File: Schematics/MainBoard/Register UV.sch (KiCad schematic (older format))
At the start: 13 parts, among them J27 UV LED Connector, U14 74F161, U15 74LS245, U16 74F161, U17 74LS245, U24 74F161, U25 74F161

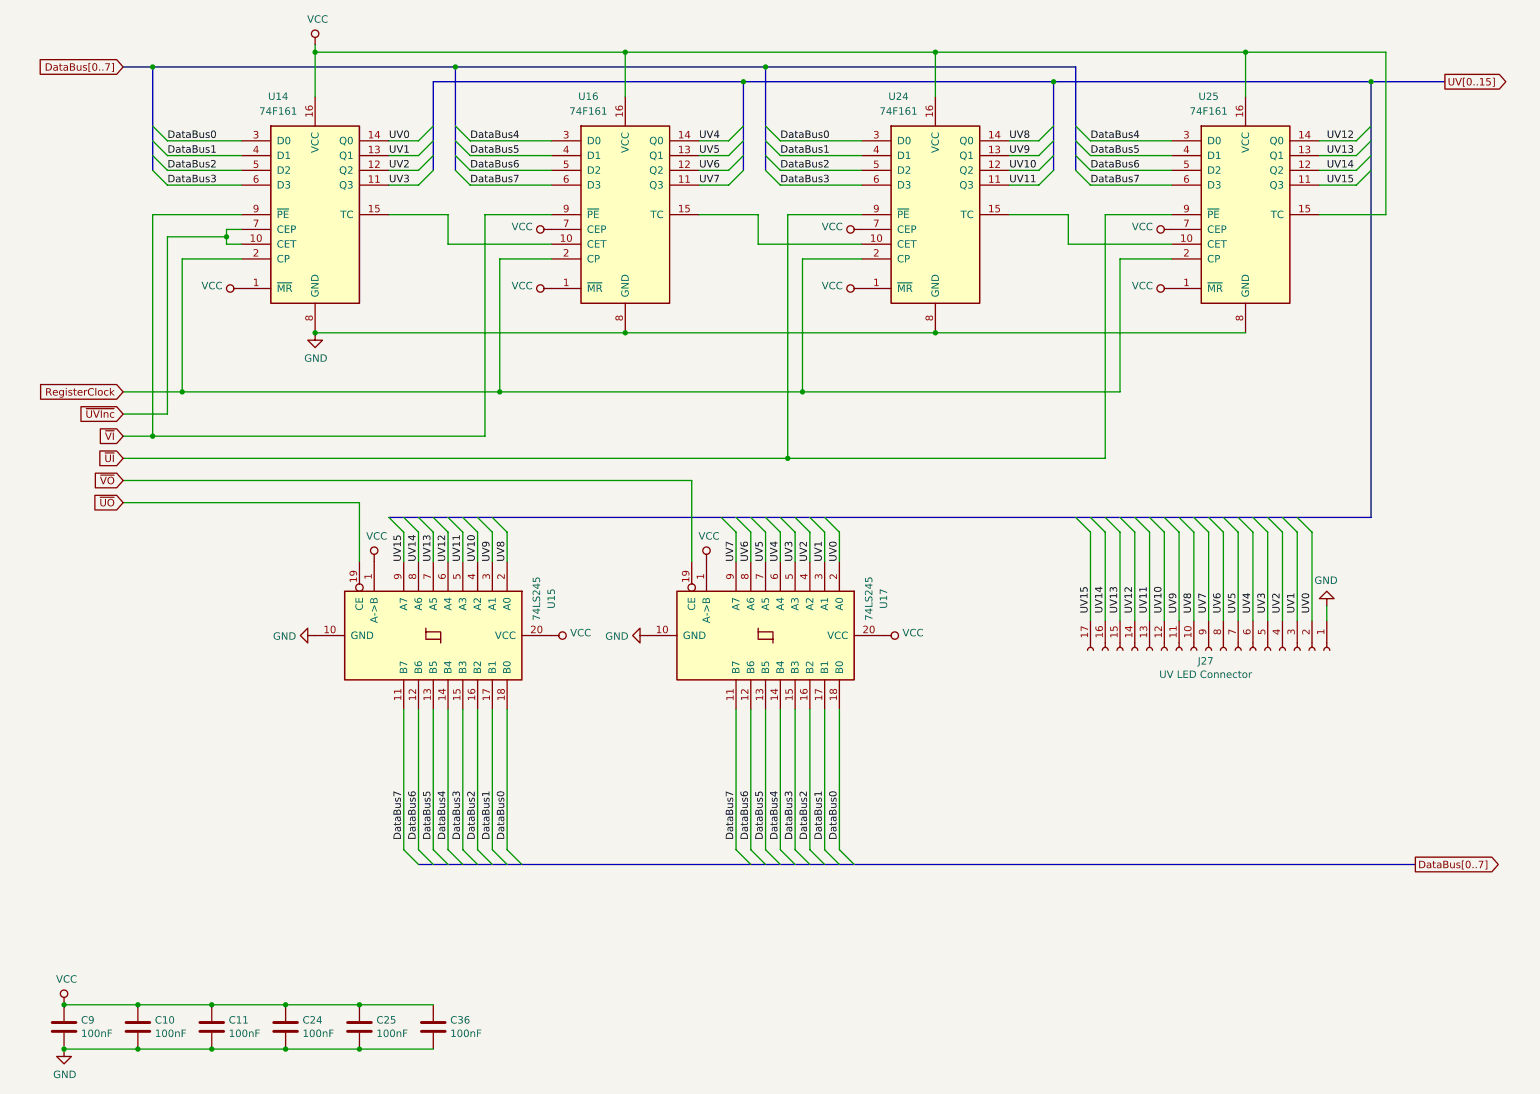
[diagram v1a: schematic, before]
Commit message: WIP: fix schematic ERC violations.
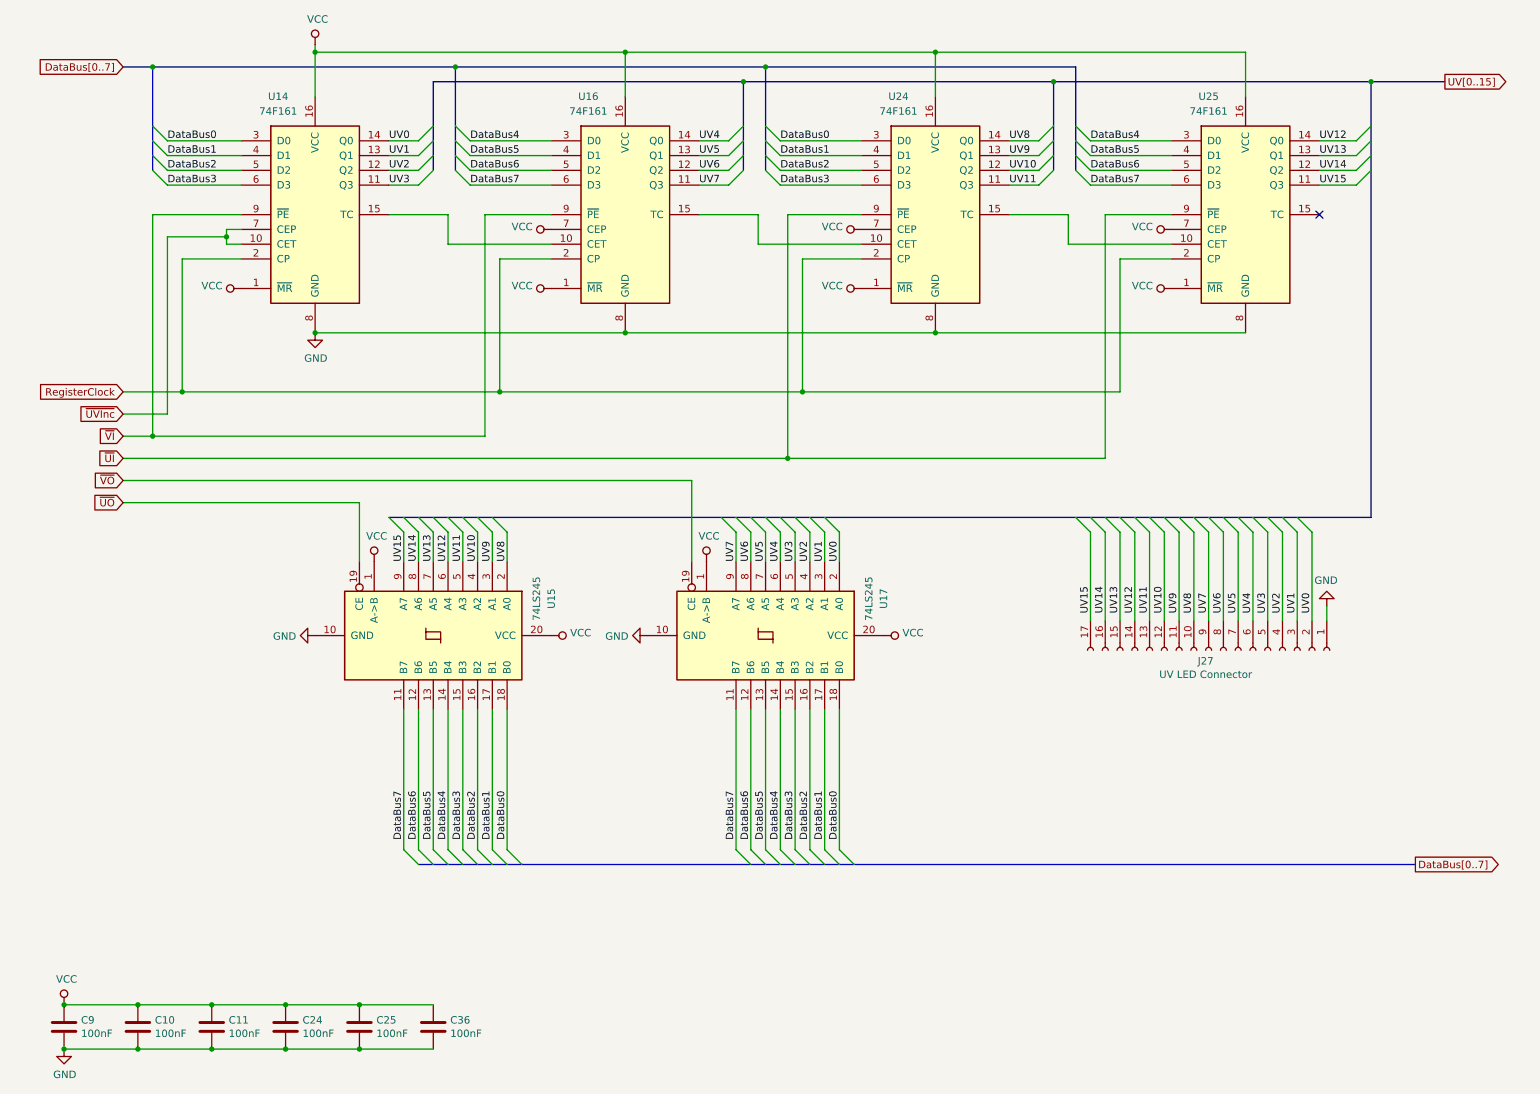
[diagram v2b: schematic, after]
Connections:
- net VCC: no longer U25.15 (TC)
- no-connect marks 0 -> 1
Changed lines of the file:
@@
 	3300 1750 3400 1650
-Wire Wire Line
-	3300 1750 3100 1750
-Wire Wire Line
-	3300 1650 3100 1650
-Wire Wire Line
-	3300 1550 3100 1550
-Wire Wire Line
-	3300 1450 3100 1450
-Text Label 3100 1450 0    50   ~ 0
-UV0
-Text Label 3100 1550 0    50   ~ 0
-UV1
 Wire Wire Line
 	1500 3450 3750 3450
@@
 	1700 3150 3850 3150
 Connection ~ 1700 3150
-Wire Wire Line
-	9850 1950 9850 850
 Entry Wire Line
 	5400 1450 5500 1350
@@
 Entry Wire Line
 	5400 1750 5500 1650
-Text Label 5200 1450 0    50   ~ 0
-UV4
-Text Label 5200 1550 0    50   ~ 0
-UV5
-Text Label 5200 1650 0    50   ~ 0
-UV6
-Text Label 5200 1750 0    50   ~ 0
-UV7
 Entry Wire Line
 	7500 1450 7600 1350
@@
 Entry Wire Line
 	7500 1750 7600 1650
-Text Label 7300 1450 0    50   ~ 0
-UV8
-Text Label 7300 1550 0    50   ~ 0
-UV9
-Text Label 7300 1650 0    50   ~ 0
-UV10
-Text Label 7300 1750 0    50   ~ 0
-UV11
 Entry Wire Line
 	9650 1450 9750 1350
@@
 Entry Wire Line
 	9650 1750 9750 1650
-Text Label 9450 1450 0    50   ~ 0
-UV12
-Text Label 9450 1550 0    50   ~ 0
-UV13
-Text Label 9450 1650 0    50   ~ 0
-UV14
-Text Label 9450 1750 0    50   ~ 0
-UV15
 Wire Bus Line
 	1300 950  1500 950
@@
 Wire Wire Line
 	7850 1450 8400 1450
-Wire Wire Line
-	9400 1950 9850 1950
-Wire Wire Line
-	9650 1450 9400 1450
-Wire Wire Line
-	9400 1550 9650 1550
-Wire Wire Line
-	9650 1650 9400 1650
-Wire Wire Line
-	9400 1750 9650 1750
 $Comp
 L 74xx:74LS161 U?
@@
 Wire Wire Line
 	6300 1550 5750 1550
-Wire Wire Line
-	7500 1450 7300 1450
-Wire Wire Line
-	7500 1550 7300 1550
-Wire Wire Line
-	7500 1650 7300 1650
-Wire Wire Line
-	7500 1750 7300 1750
 $Comp
 L 74xx:74LS161 U?
@@
 Wire Wire Line
 	4200 1450 3650 1450
-Wire Wire Line
-	5400 1450 5200 1450
-Wire Wire Line
-	5400 1550 5200 1550
-Wire Wire Line
-	5400 1650 5200 1650
-Wire Wire Line
-	5400 1750 5200 1750
 $Comp
 L 74xx:74LS161 U?
@@
 	1    0    0    -1
 $EndComp
-Text Label 3100 1750 0    50   ~ 0
-UV3
-Text Label 3100 1650 0    50   ~ 0
-UV2
 Wire Wire Line
 	7700 2150 7700 1950
@@
 Wire Wire Line
 	4700 850  6800 850
-Connection ~ 8900 850
-Wire Wire Line
-	9850 850  8900 850
 Connection ~ 4700 850
 Wire Wire Line
@@
 	0    1    1    0
 $EndComp
-Text Label 3600 4300 1    50   ~ 0
-UV11
-Text Label 3700 4300 1    50   ~ 0
-UV10
-Text Label 3900 4300 1    50   ~ 0
-UV8
-Text Label 3800 4300 1    50   ~ 0
-UV9
-Wire Wire Line
-	3600 4100 3600 4300
-Wire Wire Line
-	3700 4100 3700 4300
-Wire Wire Line
-	3800 4100 3800 4300
-Wire Wire Line
-	3900 4100 3900 4300
 Entry Wire Line
 	3900 4100 3800 4000
@@
 Entry Wire Line
 	3500 4100 3400 4000
-Text Label 3200 4300 1    50   ~ 0
-UV15
-Text Label 3300 4300 1    50   ~ 0
-UV14
-Text Label 3400 4300 1    50   ~ 0
-UV13
-Text Label 3500 4300 1    50   ~ 0
-UV12
-Wire Wire Line
-	3200 4100 3200 4300
-Wire Wire Line
-	3300 4100 3300 4300
-Wire Wire Line
-	3400 4100 3400 4300
-Wire Wire Line
-	3500 4100 3500 4300
-Text Label 5850 4300 1    50   ~ 0
-UV3
-Text Label 5950 4300 1    50   ~ 0
-UV2
-Text Label 6150 4300 1    50   ~ 0
-UV0
-Text Label 6050 4300 1    50   ~ 0
-UV1
-Wire Wire Line
-	5850 4100 5850 4300
-Wire Wire Line
-	5950 4100 5950 4300
-Wire Wire Line
-	6050 4100 6050 4300
-Wire Wire Line
-	6150 4100 6150 4300
 Entry Wire Line
 	6150 4100 6050 4000
@@
 Entry Wire Line
 	5750 4100 5650 4000
-Text Label 5450 4300 1    50   ~ 0
-UV7
-Text Label 5550 4300 1    50   ~ 0
-UV6
-Text Label 5650 4300 1    50   ~ 0
-UV5
-Text Label 5750 4300 1    50   ~ 0
-UV4
-Wire Wire Line
-	5450 4100 5450 4300
-Wire Wire Line
-	5550 4100 5550 4300
-Wire Wire Line
-	5650 4100 5650 4300
-Wire Wire Line
-	5750 4100 5750 4300
 Entry Wire Line
 	6150 6350 6050 6250
@@
 	0    1    1    0
 $EndComp
+Wire Wire Line
+	3100 1450 3300 1450
+Wire Wire Line
+	3300 1550 3100 1550
+Wire Wire Line
+	3100 1650 3300 1650
+Wire Wire Line
+	3300 1750 3100 1750
+Wire Wire Line
+	5200 1450 5400 1450
+Wire Wire Line
+	5400 1550 5200 1550
+Wire Wire Line
+	5200 1650 5400 1650
+Wire Wire Line
+	5400 1750 5200 1750
+Wire Wire Line
+	7300 1450 7500 1450
+Wire Wire Line
+	7500 1550 7300 1550
+Wire Wire Line
+	7300 1650 7500 1650
+Wire Wire Line
+	7500 1750 7300 1750
+Wire Wire Line
+	9400 1450 9650 1450
+Wire Wire Line
+	9650 1550 9400 1550
+Wire Wire Line
+	9400 1650 9650 1650
+Wire Wire Line
+	9400 1750 9650 1750
+Wire Wire Line
+	5450 4100 5450 4300
+Wire Wire Line
+	5550 4100 5550 4300
+Wire Wire Line
+	5650 4100 5650 4300
+Wire Wire Line
+	5750 4100 5750 4300
+Wire Wire Line
+	5850 4100 5850 4300
+Wire Wire Line
+	5950 4100 5950 4300
+Wire Wire Line
+	6050 4300 6050 4100
+Wire Wire Line
+	6150 4300 6150 4100
+Wire Wire Line
+	3900 4300 3900 4100
+Wire Wire Line
+	3800 4100 3800 4300
+Wire Wire Line
+	3700 4300 3700 4100
+Wire Wire Line
+	3600 4100 3600 4300
+Wire Wire Line
+	3500 4300 3500 4100
+Wire Wire Line
+	3400 4300 3400 4100
+Wire Wire Line
+	3300 4100 3300 4300
+Wire Wire Line
+	3200 4300 3200 4100
+Text Label 6150 4300 1    50   ~ 0
+UV0
+Text Label 6050 4300 1    50   ~ 0
+UV1
+Text Label 5950 4300 1    50   ~ 0
+UV2
+Text Label 5850 4300 1    50   ~ 0
+UV3
+Text Label 5750 4300 1    50   ~ 0
+UV4
+Text Label 5650 4300 1    50   ~ 0
+UV5
+Text Label 5550 4300 1    50   ~ 0
+UV6
+Text Label 5450 4300 1    50   ~ 0
+UV7
+Text Label 3900 4300 1    50   ~ 0
+UV8
+Text Label 3800 4300 1    50   ~ 0
+UV9
+Text Label 3700 4300 1    50   ~ 0
+UV10
+Text Label 3600 4300 1    50   ~ 0
+UV11
+Text Label 3500 4300 1    50   ~ 0
+UV12
+Text Label 3400 4300 1    50   ~ 0
+UV13
+Text Label 3300 4300 1    50   ~ 0
+UV14
+Text Label 3200 4300 1    50   ~ 0
+UV15
+Text Label 3100 1450 0    50   ~ 0
+UV0
+Text Label 3100 1550 0    50   ~ 0
+UV1
+Text Label 3100 1650 0    50   ~ 0
+UV2
+Text Label 3100 1750 0    50   ~ 0
+UV3
+Text Label 5200 1450 0    50   ~ 0
+UV4
+Text Label 5200 1550 0    50   ~ 0
+UV5
+Text Label 5200 1650 0    50   ~ 0
+UV6
+Text Label 5200 1750 0    50   ~ 0
+UV7
+Text Label 7300 1450 0    50   ~ 0
+UV8
+Text Label 7300 1550 0    50   ~ 0
+UV9
+Text Label 7300 1650 0    50   ~ 0
+UV10
+Text Label 7300 1750 0    50   ~ 0
+UV11
+Text Label 9400 1450 0    50   ~ 0
+UV12
+Text Label 9400 1550 0    50   ~ 0
+UV13
+Text Label 9400 1650 0    50   ~ 0
+UV14
+Text Label 9400 1750 0    50   ~ 0
+UV15
+NoConn ~ 9400 1950
+Wire Bus Line
+	9750 1050 9750 4000
 Wire Bus Line
 	7600 1050 7600 1650
@@
 	1500 950  1500 1650
 Wire Bus Line
-	9750 1050 9750 4000
-Wire Bus Line
 	3300 6350 10050 6350

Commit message: Rename UVInc and XYInc to mark them as active-high, not active-low.
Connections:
- net ~UVInc renamed UVInc
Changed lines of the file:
@@
 	7950 1950 8400 1950
 Text GLabel 1300 3300 0    50   Input ~ 0
-~UVInc
+UVInc
 Wire Wire Line
 	1600 2100 1600 3300

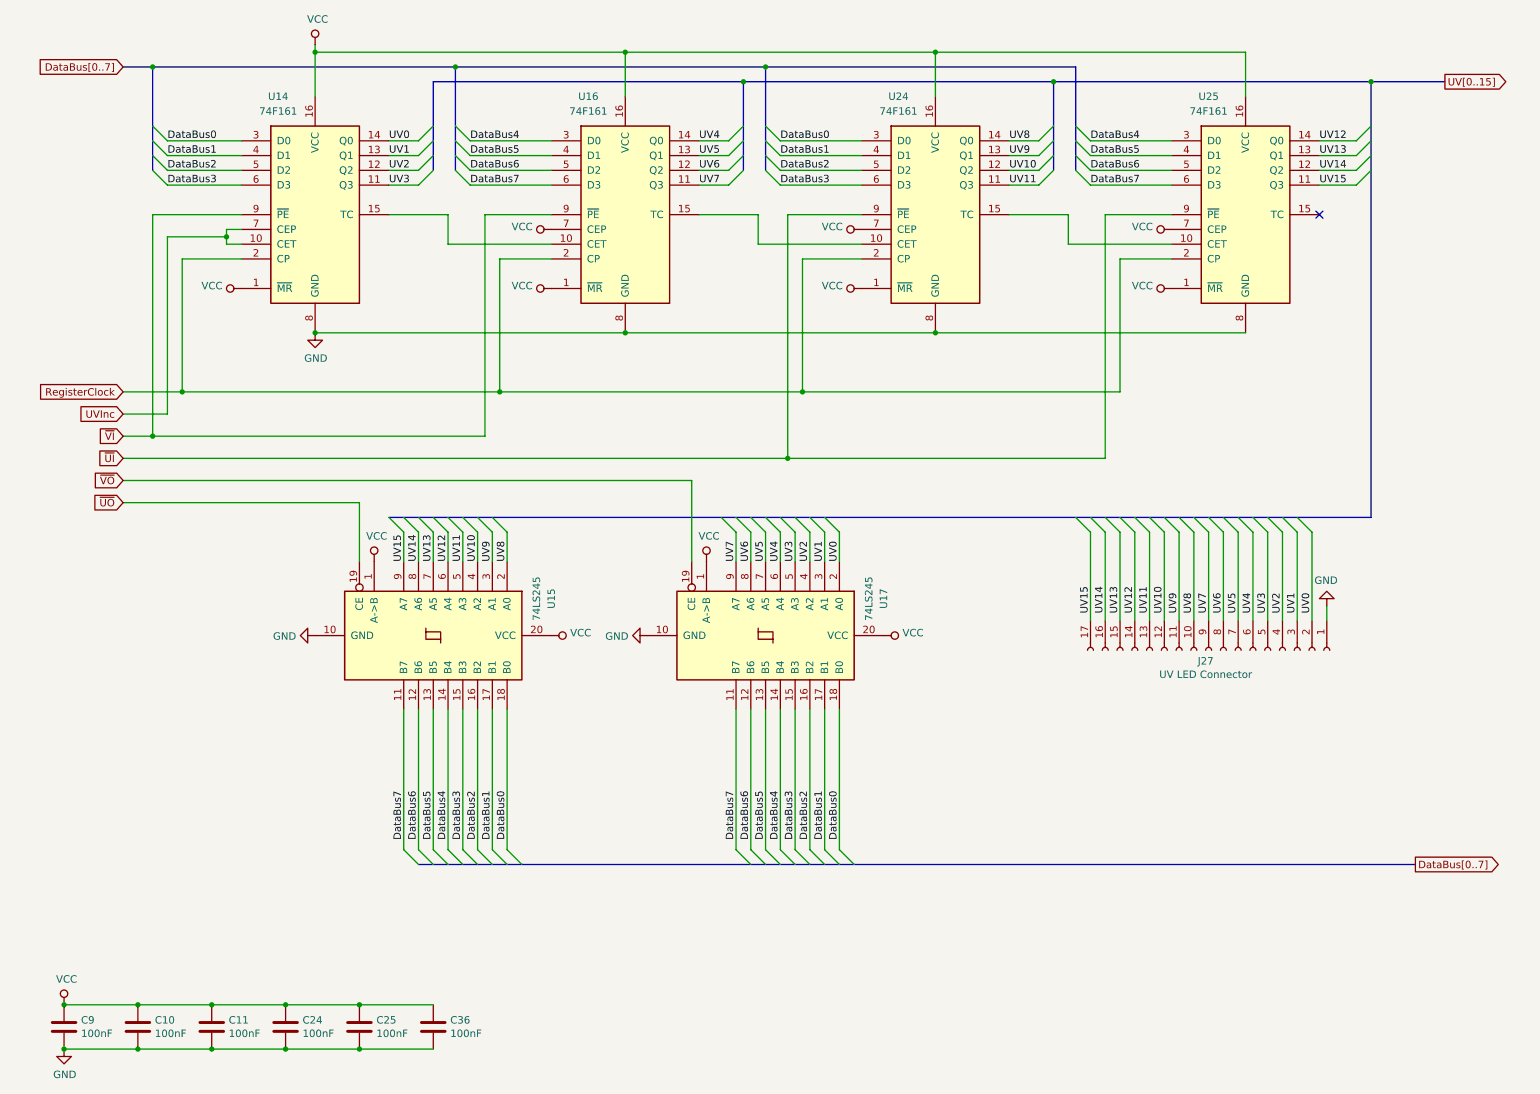
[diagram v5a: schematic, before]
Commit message: Begin work on the Rev 2 hardware.
* Four layer PCB for the main board
* Breaking the main board up into several smaller daughter boaeds.
* ZIF sockets for Instruction ROM
* Dual Port SRAM for Instruction RAM
* Daughter board connectors interleave signals and GND.
* DC Barrel jack connector for power
* WIP shifter circuit
* Rename SharedMemoryArduinoSerialCard to SerialCard.
* TurtleTTL Rev 2 will use the shared memory serial card.
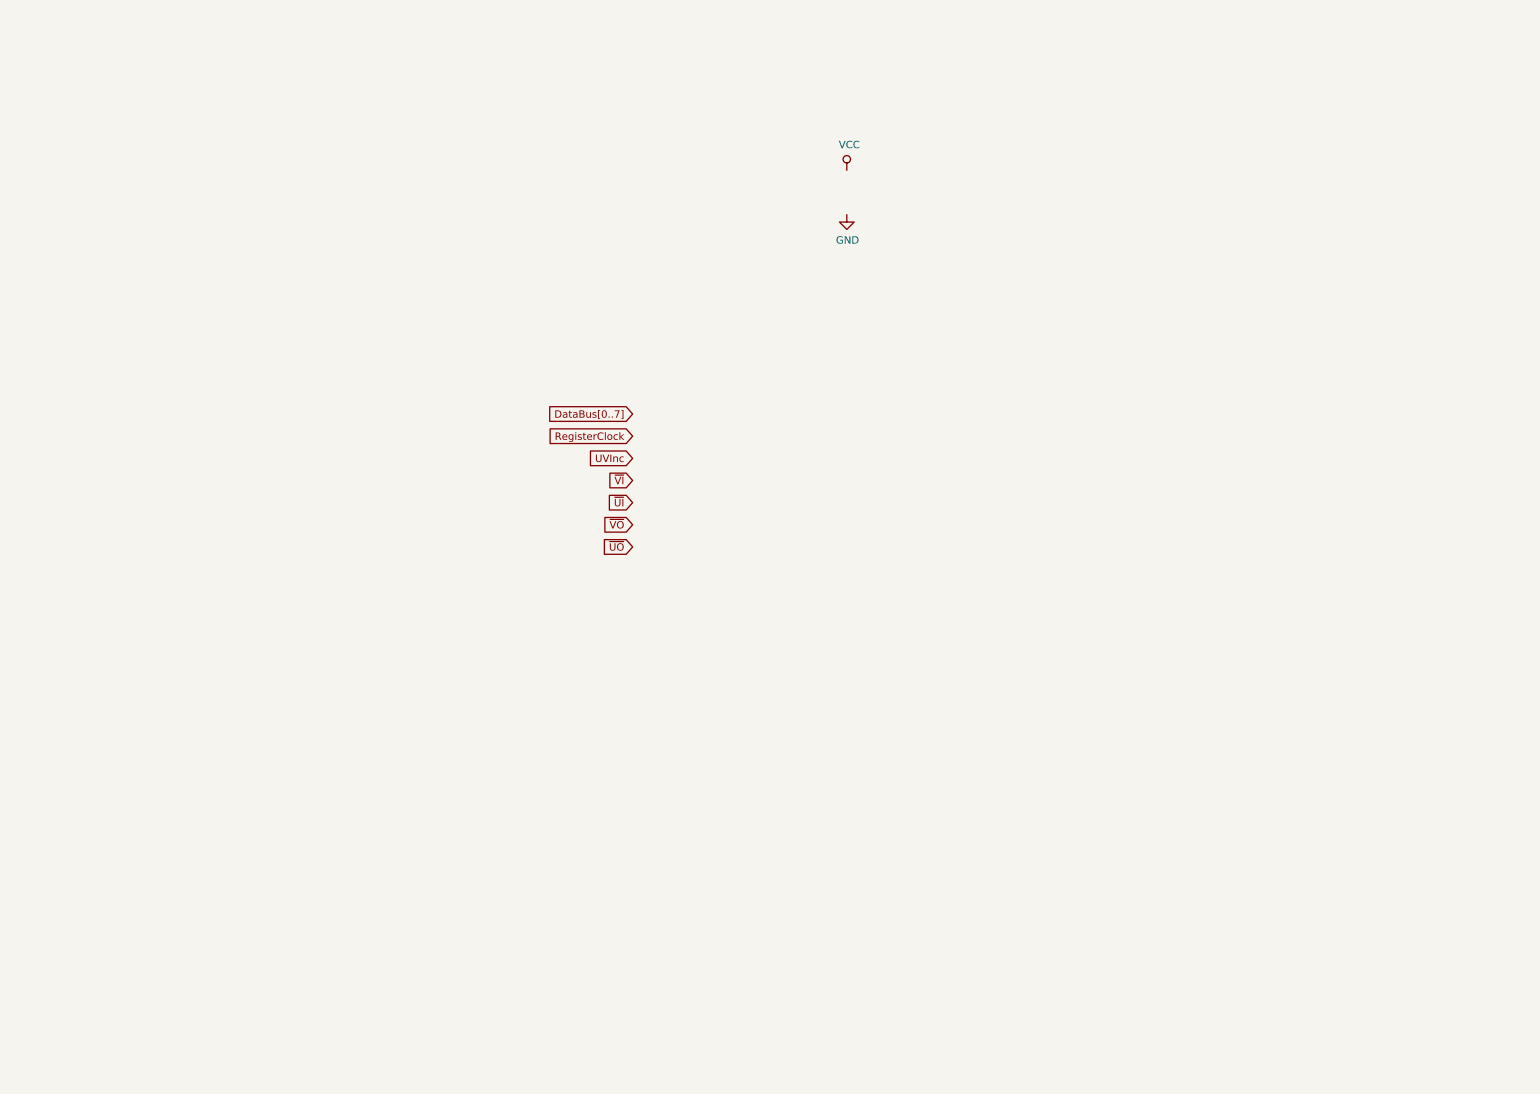
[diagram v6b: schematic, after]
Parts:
- removed C10, C11, C24, C25, C36, C9: 100nF, Capacitor_THT:C_Disc_D4.3mm_W1.9mm_P5.00mm, symbol Device:C
- removed J27: UV LED Connector, Connector_PinSocket_2.54mm:PinSocket_1x17_P2.54mm_Vertical, symbol Connector:Conn_01x17_Female
- removed U14, U16, U24, U25: 74F161, Package_DIP:DIP-16_W7.62mm, symbol 74xx:74LS161
- removed U15, U17: 74LS245, Package_DIP:DIP-20_W7.62mm, symbol 74xx:74LS245
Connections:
- no-connect marks 1 -> 0
